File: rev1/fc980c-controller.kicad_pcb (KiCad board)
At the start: 2 copper layers, 82.2 x 35.5 mm, 32 parts, among them J1 SWD, J2 USB, J3 KEYBOARD, SW1 BOOT0, U1 XC6206P332MR, U2 STM32F401CBUx, U3 USBLC6-2SC6, U5 PCA9306DC, Y1 8MHz C_l 20pF

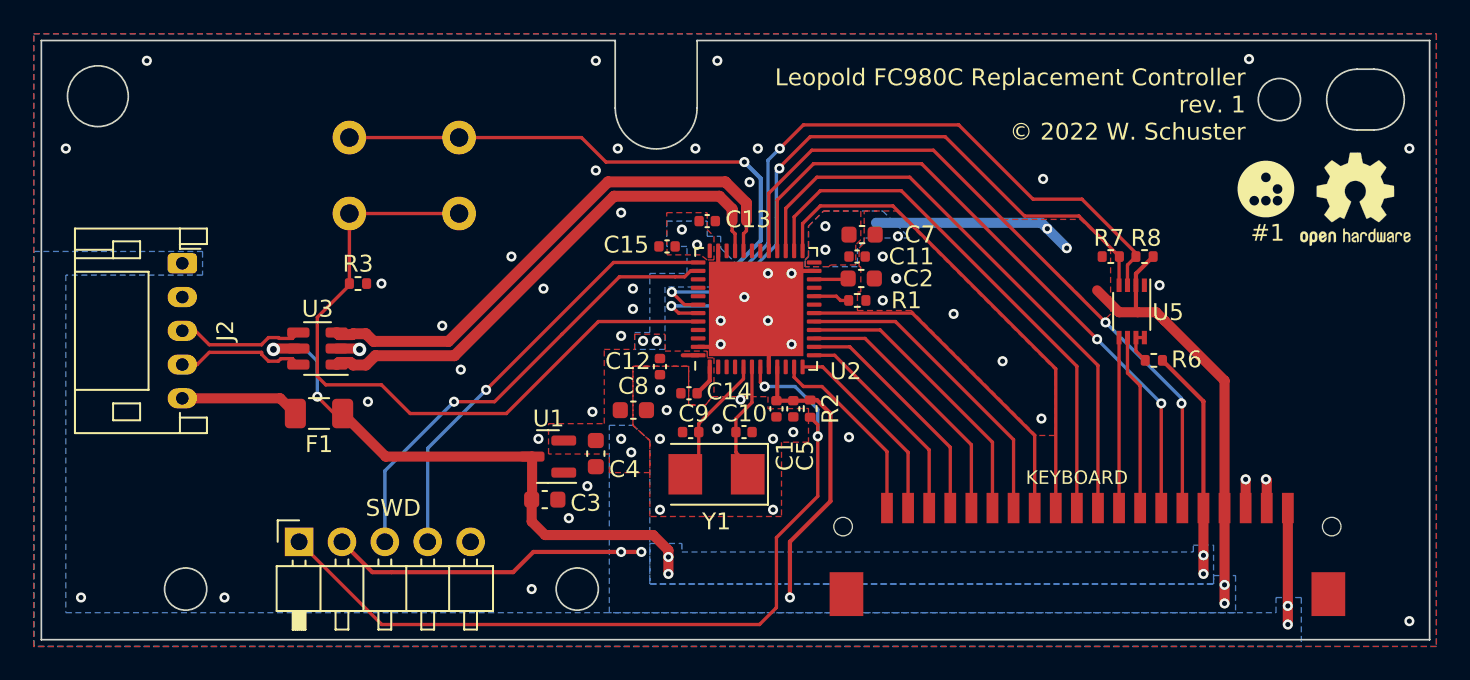
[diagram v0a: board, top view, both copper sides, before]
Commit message: rev1: Add EEPROM
This should alleviate needing to use MCU flash for EEPROM emulation.

Also recalculate crystal load capacitor values using guidance from the
MCU datasheet.
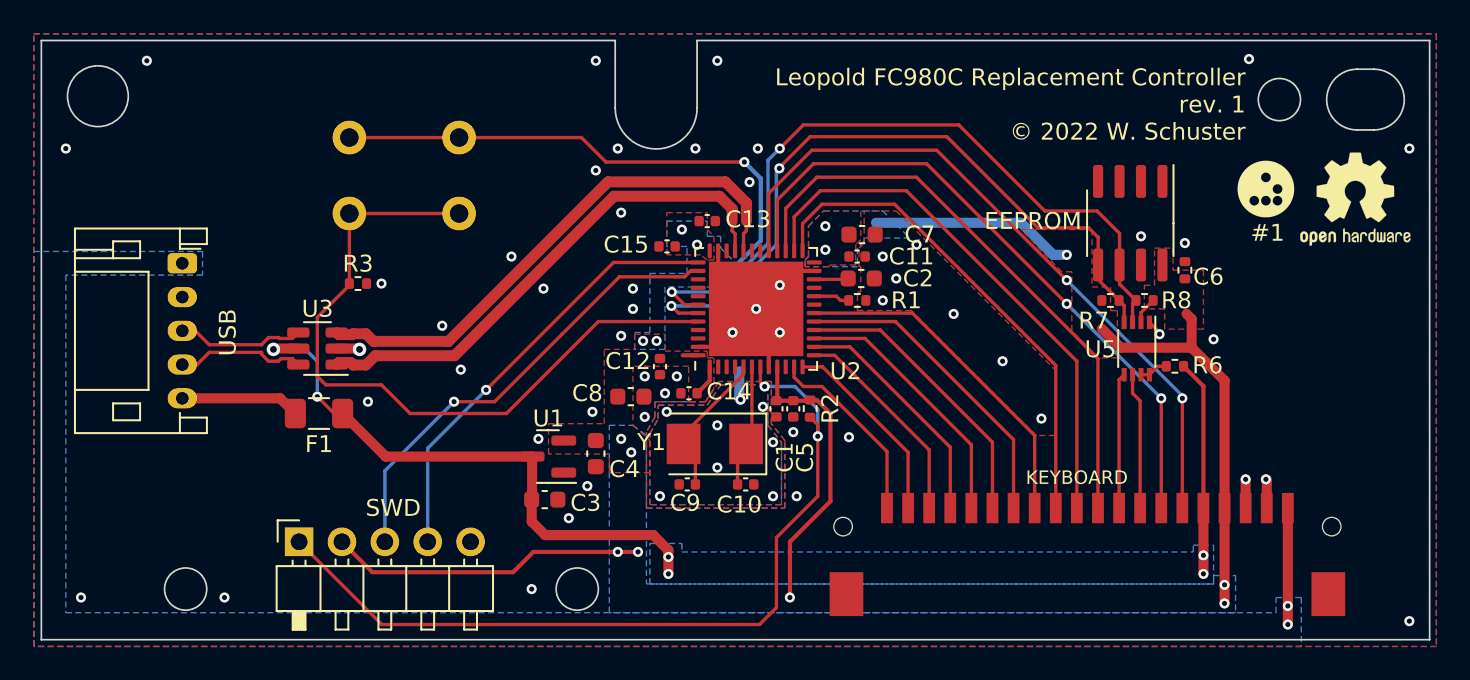
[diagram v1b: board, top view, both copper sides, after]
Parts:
- added C6: 100nF, Resistor_SMD:R_0402_1005Metric, F.Cu at (142.5, 49.1)
- added U4: M24C64-RMN6TP, Package_SO:SOIC-8_3.9x4.9mm_P1.27mm, F.Cu at (139.3, 46.3)
- C10, C9: value 30pF -> 20pF
- Y1: value 8MHz C_l 20pF -> 8MHz Cl 20pF
- moved C9 3.11 mm to (113.0, 61.8)
- moved C10 3.10 mm to (116.5, 61.8)
- moved R7 2.60 mm to (138.1, 50.9)
- moved R8 2.60 mm to (140.1, 50.9)
- moved U5 2.22 mm to (139.7, 53.8)
- moved Y1 1.80 mm to (114.7, 59.4)
- moved R6 1.30 mm to (141.9, 54.8)
- moved C8 0.81 mm to (109.7, 56.6)
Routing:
- net I2C_SCL: track 10.4 -> 8.09 mm
- net I2C_SDA_MCU: track 39.7 -> 41.9 mm
- net I2C_SCL_MCU: track 41.6 -> 43.8 mm
- net GND: track 22.5 -> 24.5 mm, vias 58 -> 62
- net I2C_SDA: track 10.1 -> 8.02 mm
- net VDDA: track 109.9 -> 108.6 mm, vias 16 -> 15
- net +5V: track 48.4 -> 47.5 mm
- net XTAL_IN: track 7.79 -> 8.64 mm
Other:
- board text added: "Licensed under CERN-OHL-S v2 l.rot13.io/fc980c-pcb Thank you to hasu and collaborators for their reverse engineering work."
- board text removed: "Licensed under CERN-OHL-S v2 l.rot13.io/fc980c-pcb Thank you to hasu and collaborators for their prior reverse engineering work."
